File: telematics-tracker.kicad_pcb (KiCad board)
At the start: 4 copper layers, 0 parts

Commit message: M4 stage 1: board foundation - outline, mounting holes, netclasses, DRC rules
tools/pcbgen.py builds telematics-tracker.kicad_pcb from a pristine template
the same way tools/sheets.py builds the sheets. Provisional 80 x 60 mm rounded
outline, 4 corner M3 holes GND-tied, HV ZONE silk boundary at x = 20 mm.

Fifth M3 hole added at (27, 52) for F-18 - see design-log. None of the four
corner holes is usable as the IMU anchor: two sit inside the HV strip and two
in the RF corners beside the U.FL connectors. A digital-zone standoff also
stiffens the panel under the 31 x 28 mm LCC module, which matters for solder
joint life under MEWP vibration. Provisional like the outline: needs a matching
boss in the purchased housing.

Netclasses added to the project with pattern assignment (32 patterns):
  RF          track 0.40, clearance 0.30  - the computed 50 ohm CPWG geometry
  HV          track 0.50, clearance 0.60  - IPC-2221 external uncoated at 100 V
  MODEM_BULK  track 2.00                  - handoff section 4 minimum
  PWR         track 0.50
  GND         own class so the HV-to-LV rule can except it
telematics-tracker.kicad_dru adds the rules a netclass cannot express, chiefly
the directional HV-to-signal 1.5 mm separation (handoff section 7) which must
except GND, since D2/C70-C74/R80 all return to GND right beside their HV pads.

Two pcbnew traps hit and worked around, both documented in the code:
  - board.Remove() hands ownership back to Python and double-frees, segfaulting
    the interpreter on the next GC. The generator never deletes; it rebuilds
    from tools/pcb-template.kicad_pcb.
  - KIIDs are random with no Python setter, and footprints are written from an
    unordered container, so plain regeneration produced reordered blocks and
    fresh uuids every run. canonicalise() sorts top-level forms by a stable key
    and restamps uuids by position, keeping the board byte-stable so
    MIGRATION.md's "regenerate then git diff must be empty" check still works.

Veri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
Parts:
- added H1: MountingHole_3.2mm_M3_ISO7380_Pad, MountingHole_3.2mm_M3_ISO7380_Pad, F.Cu at (3.50, 3.50)
- added H2: MountingHole_3.2mm_M3_ISO7380_Pad, MountingHole_3.2mm_M3_ISO7380_Pad, F.Cu at (76.5, 3.50)
- added H3: MountingHole_3.2mm_M3_ISO7380_Pad, MountingHole_3.2mm_M3_ISO7380_Pad, F.Cu at (3.50, 56.5)
- added H4: MountingHole_3.2mm_M3_ISO7380_Pad, MountingHole_3.2mm_M3_ISO7380_Pad, F.Cu at (76.5, 56.5)
- added H5: MountingHole_3.2mm_M3_ISO7380_Pad, MountingHole_3.2mm_M3_ISO7380_Pad, F.Cu at (27.0, 52.0)
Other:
- board outline added: 80 x 60 mm
- board text added: "HV ZONE <= 100 V"

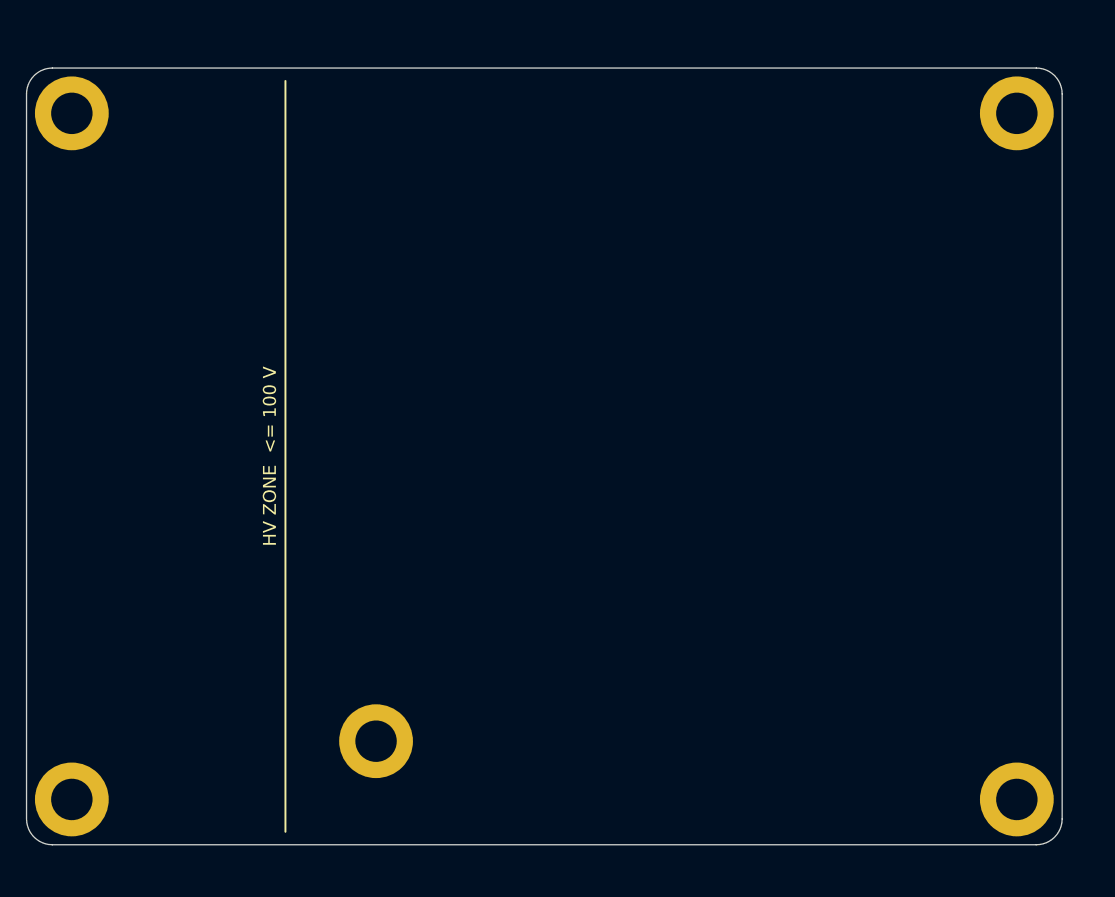
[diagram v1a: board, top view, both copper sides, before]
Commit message: M4 stage 2: F-13, F-16, F-17 closed; full placement + planes (NOT routed)
F-13 APPLIED (no waiver): VBAT_MODEM bulk 2x 100uF 6.3V X5R (C49066, which
broke rule 1 twice - X5R, and 6.3/4.35 = 1.45:1 not >=2:1) -> 4x 47uF 10V X7R
Murata GRM32ER71A476KE15L (C84494), refs C40/C41/C81/C82. 27.97uF per part read
at exact 4.35V/85.0C grid points from Murata's simulation backend = 111.9uF
effective, 2.30:1 derating. Cross-validated within ~7% by Taiyo Yuden C20486249
(second source). 10uF X5R 0805 -> C109040 X7S, +125C rated. Rule 1 now MET.
Also logged: all three previously-recorded F-13 options actually deliver only
63/76/92uF; no 100uF X7R/X7S >=10V exists in 1210/1812 from anyone; and
multiplying a 25C bias curve by a 0V temperature curve over-predicts by 9-12%.

F-17 CLOSED: derived lib/jlc.pretty/eSIM_MFF2_VFDFPN8.kicad_mod from four
independent vendor documents that publish an identical land, plus normative
ETSI TS 102 671 V12.0.0. ETSI table 6.1 confirms the schematic pinout is
correct (pins 1-8 = C5,C6,C7,C8,C4,C3,C2,C1). EP tied to GND per Infineon p.24
and numbered "1" so it merges with the GND pin. Logged as a deliberate
golden-rule-1 deviation: MFF2 is a package site, not an LCSC part, so there is
no C-number to import. This was the last unresolved footprint and the only
footprint_link_issues warning, so ERC is now 0 errors / 13 warnings.

F-16: X ambiguity RESOLVED - the incumbent's 8.50 is post-to-post centres, and
the earlier reading of 2.50/1.22 as post positions was wrong (they are the
bottom-pad chain). Y remains genuinely ambiguous. Three vendors (GCT, HRO,
Megastar) publish an identical scheme giving Y = +1.25; GCT's numbers were
re-extracted and verified locally. Megastar C7419882 (+13%) is fully
dimensioned BUT easyeda2kicad has no data for it, so switching means a
hand-drawn footprint - held for the user rather than trading a verified
imported footprint for a documented hand-drawn one. SIM area reserved with the
incumbent pad map and NO post holes, so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
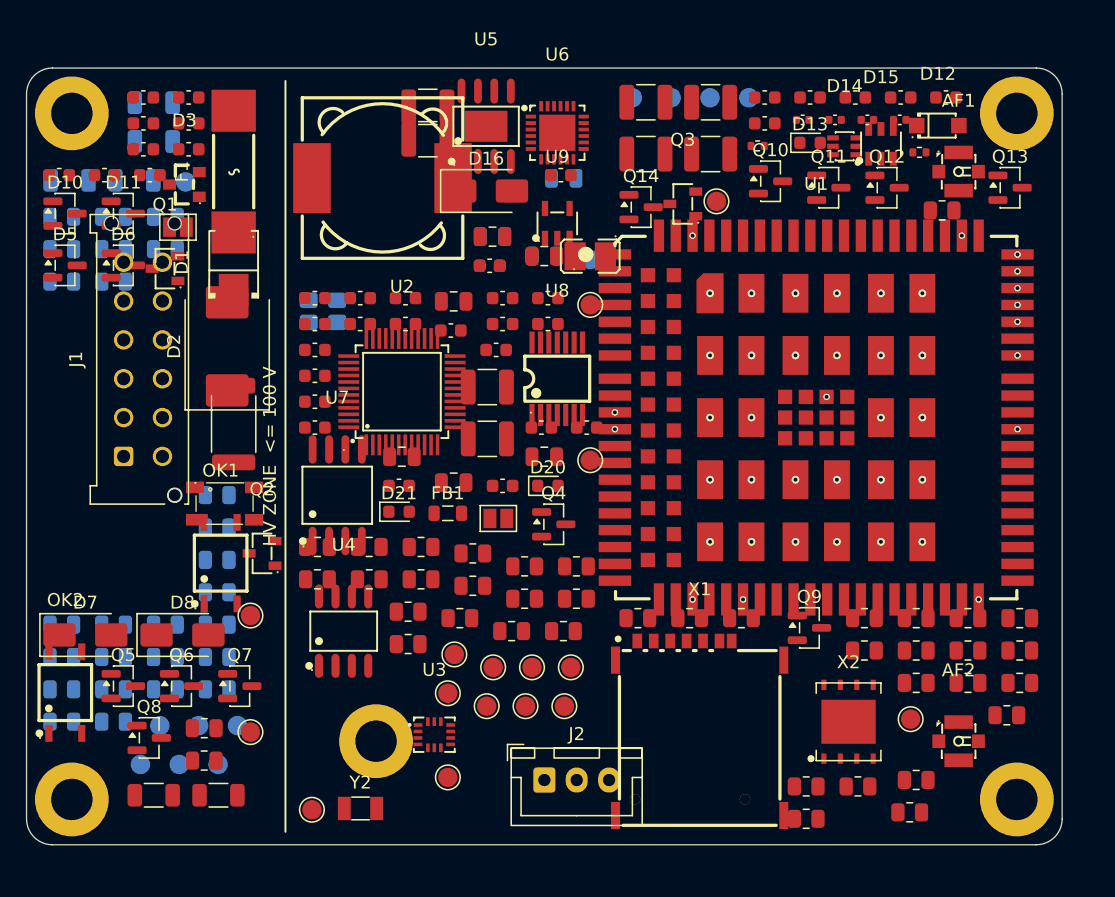
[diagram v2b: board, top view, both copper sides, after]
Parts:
- added AF2: U.FL, CONN-SMD_XY-IPEX1, F.Cu at (72.0, 52.0)
- added C1: 18pF, C_0603_1608Metric, F.Cu at (22.3, 17.8)
- added C10: 100nF, C_0603_1608Metric, F.Cu at (25.8, 17.8)
- added C11: 100nF, C_0603_1608Metric, F.Cu at (29.3, 17.8)
- added C12: 4.7uF, C_0805_2012Metric, F.Cu at (33.0, 18.0)
- added C13: 100nF, C_0603_1608Metric, F.Cu at (36.8, 17.8)
- added C14: 1uF, C_0603_1608Metric, F.Cu at (40.3, 17.8)
- added C2: 18pF, C_0603_1608Metric, F.Cu at (22.3, 19.8)
- added C20: 100nF, C_0603_1608Metric, F.Cu at (25.8, 19.8)
- added C21: 1uF, C_0603_1608Metric, F.Cu at (29.3, 19.8)
- added C22: 4.7nF, C_0603_1608Metric, F.Cu at (9.03, 2.27)
- added C23: 100nF, C_0603_1608Metric, F.Cu at (12.5, 2.27)
- added C24: 100nF, C_0603_1608Metric, F.Cu at (9.03, 4.28)
- added C25: 100nF, C_0603_1608Metric, F.Cu at (12.5, 4.28)
- added C26: 100nF, C_0603_1608Metric, F.Cu at (9.03, 6.28)
- added C27: 100nF, C_0603_1608Metric, F.Cu at (12.5, 6.28)
- added C28: 100nF, C_0603_1608Metric, F.Cu at (2.52, 8.28)
- added C29: 100nF, C_0603_1608Metric, F.Cu at (6.03, 8.28)
- added C3: 6.8pF, C_0603_1608Metric, F.Cu at (36.8, 19.8)
- added C30: 100nF, C_0603_1608Metric, F.Cu at (9.53, 8.28)
- added C4: 6.8pF, C_0603_1608Metric, F.Cu at (40.3, 19.8)
- added C40: 47uF X7R, C_1210_3225Metric, F.Cu at (47.8, 2.65)
- added C41: 47uF X7R, C_1210_3225Metric, F.Cu at (52.8, 2.65)
- added C42: 1uF, C_0603_1608Metric, F.Cu at (57.0, 2.27)
- added C43: 100nF, C_0603_1608Metric, F.Cu at (60.5, 2.27)
- added C44: 1uF, C_0603_1608Metric, F.Cu at (64.0, 2.27)
- added C45: 100nF, C_0603_1608Metric, F.Cu at (67.5, 2.27)
- added C46: 100nF, C_0603_1608Metric, F.Cu at (71.0, 2.27)
- added C47: 100nF, C_0603_1608Metric, F.Cu at (57.0, 4.28)
- added C48: DNP, C_0402_1005Metric, F.Cu at (60.0, 4.00)
- added C49: DNP, C_0402_1005Metric, F.Cu at (62.5, 4.00)
- added C5: 100nF, C_0603_1608Metric, F.Cu at (32.8, 20.3)
- added C50: DNP, C_0402_1005Metric, F.Cu at (65.0, 4.00)
- added C51: DNP, C_0402_1005Metric, F.Cu at (67.5, 4.00)
- added C6: 100nF, C_0603_1608Metric, F.Cu at (22.3, 21.8)
- added C61: 1uF, C_0603_1608Metric, F.Cu at (41.3, 8.28)
- added C62: 10uF, C_0805_2012Metric, F.Cu at (36.0, 13.0)
- added C63: 4.7uF, C_0805_2012Metric, F.Cu at (40.0, 14.5)
- added C64: 47nF, C_0603_1608Metric, F.Cu at (35.8, 15.3)
- added C65: 10uF, C_0805_2012Metric, B.Cu at (41.5, 8.53)
- added C66: 10uF, C_0805_2012Metric, B.Cu at (36.0, 13.0)
- added C67: 10uF, C_0805_2012Metric, B.Cu at (40.0, 14.5)
- added C68: 1uF, C_0603_1608Metric, B.Cu at (35.8, 15.3)
- added C69: 1uF, C_0603_1608Metric, F.Cu at (36.3, 21.8)
- added C7: 1uF, C_0603_1608Metric, F.Cu at (22.3, 23.8)
- added C70: 2.2uF 100V, C_1210_3225Metric, F.Cu at (35.6, 24.6)
- added C71: 2.2uF 100V, C_1210_3225Metric, F.Cu at (35.6, 28.6)
- added C72: 100nF, C_0603_1608Metric, F.Cu at (22.3, 25.8)
- added C73: 2.2uF 100V, C_1210_3225Metric, F.Cu at (31.0, 3.00)
- added C74: 2.2uF 100V, C_1210_3225Metric, F.Cu at (31.0, 5.50)
- added C75: 1uF 25V, C_0603_1608Metric, F.Cu at (22.3, 27.8)
- added C76: 100nF 25V, C_0603_1608Metric, F.Cu at (39.8, 27.8)
- added C77: 10uF, C_0805_2012Metric, F.Cu at (29.0, 30.0)
- added C78: 10uF, C_0805_2012Metric, F.Cu at (40.0, 30.0)
- added C79: 10uF, C_0805_2012Metric, F.Cu at (33.0, 32.0)
- added C8: 100nF, C_0603_1608Metric, F.Cu at (43.3, 27.8)
- added C80: 100nF, C_0603_1608Metric, F.Cu at (28.8, 32.3)
- added C81: 47uF X7R, C_1210_3225Metric, F.Cu at (47.8, 6.64)
- added C82: 47uF X7R, C_1210_3225Metric, F.Cu at (52.8, 6.64)
- added C9: 100nF, C_0603_1608Metric, F.Cu at (36.8, 32.3)
- added D1: S3M, SMB_L4.3-W3.6-LS5.3-RD, F.Cu at (16.0, 15.0)
- added D10: BAV99, SOT-23, F.Cu at (2.98, 11.2)
- added D11: BAV99, SOT-23, F.Cu at (7.47, 11.2)
- added D12: SMF5.0A, SOD-123FL_L2.7-W1.8-LS3.8-RD, F.Cu at (70.4, 4.45)
- added D13: NET, LED_0603_1608Metric, F.Cu at (60.5, 5.78)
- added D14: SMF05C, SOT-363_L2.0-W1.3-P0.65-LS2.1-BR, F.Cu at (63.2, 6.04)
- added D15: USBLC6-2SC6, SOT-23-6_L2.9-W1.6-P0.95-LS2.8-BL, F.Cu at (66.0, 5.86)
- added D16: SS3200, D_SMA, F.Cu at (35.5, 9.50)
- added D2: SMDJ100A, D_SMC, F.Cu at (15.5, 21.5)
- added D20: GRN, LED_0603_1608Metric, F.Cu at (40.3, 32.3)
- added D21: BLU, LED_0603_1608Metric, F.Cu at (28.8, 34.3)
- added D3: PESD1CAN, SOT-23_L2.9-W1.3-P1.90-LS2.4-BR, F.Cu at (12.2, 8.99)
- added D5: BAV99, SOT-23, F.Cu at (2.98, 15.2)
- added D6: BAV99, SOT-23, F.Cu at (7.47, 15.2)
- added D7: SS3200, D_SMA, F.Cu at (4.54, 43.8)
- added D8: SS3200, D_SMA, F.Cu at (12.0, 43.8)
- added F1: 1A 250V, FUSE-SMD_L10.1-W3.1, F.Cu at (16.0, 8.00)
- added FB1: 600R@100MHz, L_0805_2012Metric, F.Cu at (32.5, 34.4)
- added H1: MountingHole_3.2mm_M3_ISO7380_Pad, MountingHole_3.2mm_M3_ISO7380_Pad, F.Cu at (3.50, 3.50)
- added J1: WAFER-MX3.0-12PZZ, XUNPU_MX3.0-12PZZ_2x06_P3.00mm_Vertical, F.Cu at (7.50, 30.0)
- added J2: B3B-XH-A, JST_XH_B3B-XH-A_1x03_P2.50mm_Vertical, F.Cu at (40.0, 55.0)
- added JP1: BOOT0_SEL, SolderJumper-2_P1.3mm_Open_Pad1.0x1.5mm, F.Cu at (36.4, 34.8)
- added JP2: CAN_TERM, SolderJumper-2_P1.3mm_Open_Pad1.0x1.5mm, F.Cu at (11.7, 12.3)
- added L1: 150uH 2.7A, IND-SMD_L12.3-W12.3, F.Cu at (27.5, 8.50)
- added L2: ACT45B-510-2P, IND-SMD_4P-L4.5-W3.2-TL, F.Cu at (15.3, 33.6)
- added L3: 2.2uH, L1008, F.Cu at (43.5, 14.5)
- added OK1: EL357N(D), OPTO-SMD-4_L4.4-W4.1-P2.54-LS7.0-BL, F.Cu at (15.0, 38.2)
- added OK2: EL357N(D), OPTO-SMD-4_L4.4-W4.1-P2.54-LS7.0-BL, F.Cu at (3.00, 48.2)
- added Q1: AM2390N-TP, SOT-23-3_L2.9-W1.3-P1.90-LS2.4-BR, F.Cu at (10.7, 15.5)
- added Q10: MMBT3904, SOT-23, F.Cu at (57.5, 8.74)
- added Q11: MMBT3904, SOT-23, F.Cu at (62.0, 9.24)
- added Q12: MMBT3904, SOT-23, F.Cu at (66.5, 9.24)
- added Q13: MMBT3906, SOT-23, F.Cu at (76.0, 9.24)
- added Q14: MMBT3904, SOT-23, F.Cu at (47.5, 10.7)
- added Q2: AM2390N-TP, SOT-23-3_L2.9-W1.3-P1.90-LS2.4-BR, F.Cu at (18.2, 37.5)
- added Q3: AO3401A, SOT-23-3_L2.9-W1.3-P1.90-LS2.4-BR, F.Cu at (50.7, 10.5)
- added Q4: MMBT3904, SOT-23, F.Cu at (40.7, 35.2)
- added Q5: MMBT3904, SOT-23, F.Cu at (7.47, 47.7)
- added Q6: MMBT3904, SOT-23, F.Cu at (12.0, 47.7)
- added Q7: MMBT3904, SOT-23, F.Cu at (16.5, 47.7)
- added Q8: MMBT3904, SOT-23, F.Cu at (9.47, 51.7)
- added Q9: MMBT3904, SOT-23, F.Cu at (60.5, 43.2)
- added R1: 10k, R_0805_2012Metric, F.Cu at (22.5, 37.0)
- added R11: 60.4R, R_0805_2012Metric, F.Cu at (13.7, 51.0)
- added R12: 60.4R, R_0805_2012Metric, F.Cu at (13.7, 53.5)
- added R14: 12k, R_1206_3216Metric, F.Cu at (9.82, 56.2)
- added R15: 12k, R_1206_3216Metric, F.Cu at (14.8, 56.2)
- added R16: 12k, R_1206_3216Metric, B.Cu at (9.82, 2.67)
- added R17: 12k, R_1206_3216Metric, B.Cu at (9.82, 5.67)
- added R18: 12k, R_1206_3216Metric, B.Cu at (3.33, 8.68)
- added R19: 12k, R_1206_3216Metric, B.Cu at (8.32, 8.68)
- added R2: 10k, R_0805_2012Metric, F.Cu at (26.5, 37.0)
- added R21: 47k, R_0805_2012Metric, B.Cu at (2.73, 11.5)
- added R22: 47k, R_0805_2012Metric, B.Cu at (6.72, 11.5)
- added R23: 100R, R_0805_2012Metric, B.Cu at (10.7, 11.5)
- added R24: 100R, R_0805_2012Metric, B.Cu at (2.73, 14.0)
- added R25: 10k, R_0805_2012Metric, B.Cu at (6.72, 14.0)
- added R26: 10k, R_0805_2012Metric, B.Cu at (10.7, 14.0)
- added R3: 0R, R_0805_2012Metric, F.Cu at (30.5, 37.0)
- added R30: 100k, R_0805_2012Metric, B.Cu at (2.73, 16.5)
- added R31: 100k, R_0805_2012Metric, B.Cu at (6.72, 16.5)
- added R32: 100k, R_0805_2012Metric, B.Cu at (14.7, 33.0)
- added R33: 100k, R_0805_2012Metric, B.Cu at (14.7, 35.5)
- added R34: 100k, R_0805_2012Metric, B.Cu at (14.7, 38.0)
- added R35: 100k, R_0805_2012Metric, B.Cu at (14.7, 40.5)
- added R36: 9.1k, R_0805_2012Metric, B.Cu at (2.73, 43.0)
- added R37: 9.1k, R_0805_2012Metric, B.Cu at (6.72, 43.0)
- added R38: 1M, R_0805_2012Metric, B.Cu at (10.7, 43.0)
- added R39: 1M, R_0805_2012Metric, B.Cu at (14.7, 43.0)
- added R4: 1k, R_0805_2012Metric, F.Cu at (34.5, 37.5)
- added R40: 100k, R_0805_2012Metric, B.Cu at (2.73, 45.5)
- added R41: 9.1k, R_0805_2012Metric, B.Cu at (6.72, 45.5)
- added R42: 4.7k, R_0805_2012Metric, B.Cu at (10.7, 45.5)
- added R43: 10k, R_0805_2012Metric, B.Cu at (14.7, 45.5)
- added R44: 10k, R_0805_2012Metric, B.Cu at (2.73, 48.0)
- added R45: 2.2k, R_0805_2012Metric, B.Cu at (6.72, 48.0)
- added R46: 4.7k, R_0805_2012Metric, B.Cu at (10.7, 48.0)
- added R47: 10k, R_0805_2012Metric, B.Cu at (14.7, 48.0)
- added R48: 10k, R_0805_2012Metric, B.Cu at (2.73, 50.5)
- added R49: 2.2k, R_0805_2012Metric, B.Cu at (6.72, 50.5)
- added R5: 4.7k, R_0805_2012Metric, F.Cu at (38.5, 38.5)
- added R50: 100k, R_0805_2012Metric, F.Cu at (70.7, 11.0)
- added R51: 10k, R_0805_2012Metric, F.Cu at (47.2, 42.5)
- added R52: 47k, R_0805_2012Metric, F.Cu at (51.2, 42.5)
- added R53: 4.7k, R_0805_2012Metric, F.Cu at (55.2, 42.5)
- added R54: 47k, R_0805_2012Metric, F.Cu at (64.7, 42.5)
- added R55: 4.7k, R_0805_2012Metric, F.Cu at (68.7, 42.5)
- added R56: 47k, R_0805_2012Metric, F.Cu at (72.7, 42.5)
- added R57: 4.7k, R_0805_2012Metric, F.Cu at (76.7, 42.5)
- added R58: 47k, R_0805_2012Metric, F.Cu at (64.7, 45.0)
- added R59: 4.7k, R_0805_2012Metric, F.Cu at (68.7, 45.0)
- added R6: 1k, R_0805_2012Metric, F.Cu at (42.5, 38.5)
- added R60: 47k, R_0805_2012Metric, F.Cu at (72.7, 45.0)
- added R61: 47k, R_0805_2012Metric, F.Cu at (76.7, 45.0)
- added R62: 10k, R_0805_2012Metric, F.Cu at (68.7, 47.5)
- added R63: 47k, R_0805_2012Metric, F.Cu at (72.7, 47.5)
- added R64: 4.7k, R_0805_2012Metric, F.Cu at (76.7, 47.5)
- added R65: 1k, R_0805_2012Metric, F.Cu at (75.7, 50.0)
- added R66: 33R, R_0805_2012Metric, F.Cu at (68.7, 55.0)
- added R67: 33R, R_0805_2012Metric, F.Cu at (60.2, 55.5)
- added R68: 33R, R_0805_2012Metric, F.Cu at (64.2, 55.5)
- added R69: 0R, R_0805_2012Metric, F.Cu at (68.2, 57.5)
- added R7: 2.2k, R_0805_2012Metric, F.Cu at (22.5, 39.5)
- added R70: 0R, R_0805_2012Metric, F.Cu at (60.2, 58.0)
- added R71: 0R, R_0402_1005Metric, F.Cu at (56.5, 6.01)
- added R72: 0R, R_0402_1005Metric, F.Cu at (69.0, 6.51)
- added R8: 2.2k, R_0805_2012Metric, F.Cu at (26.5, 39.5)
- added R80: 1R 2512 anti-surge, R_2512_6332Metric, F.Cu at (16.0, 27.5)
- added R81: 100k, R_0805_2012Metric, F.Cu at (30.5, 39.5)
- added R82: 0R (F-12), R_0805_2012Metric, F.Cu at (34.5, 40.0)
- added R83: 4.3k, R_0805_2012Metric, F.Cu at (38.5, 41.0)
- added R84: 1.5k, R_0805_2012Metric, F.Cu at (42.5, 41.0)
- added R85: 976R, R_0805_2012Metric, F.Cu at (29.5, 42.0)
- added R86: 536R, R_0805_2012Metric, F.Cu at (33.5, 42.5)
- added R87: 10k, R_0805_2012Metric, F.Cu at (37.5, 43.5)
- added R88: 5.23k, R_0805_2012Metric, F.Cu at (41.5, 43.5)
- added R89: 30.1k, R_0805_2012Metric, F.Cu at (29.5, 44.5)
- added TP1: SWDIO, TestPoint_Pad_D1.5mm, F.Cu at (43.5, 18.3)
- added TP10: VIN_SENSE, TestPoint_Pad_D1.5mm, F.Cu at (17.3, 42.3)
- added TP11: IGN_SENSE, TestPoint_Pad_D1.5mm, F.Cu at (17.3, 51.3)
- added TP12: VBAT_SENSE, TestPoint_Pad_D1.5mm, B.Cu at (12.3, 8.80)
- added TP13: SYS, TestPoint_Pad_D1.5mm, B.Cu at (10.3, 50.8)
- added TP14: MODEM_STATUS, TestPoint_Pad_D1.5mm, F.Cu at (53.3, 10.3)
- added TP15: USB_DP_TP, TestPoint_Pad_D1.5mm, F.Cu at (68.3, 50.3)
- added TP16: USB_DM_TP, TestPoint_Pad_D1.5mm, B.Cu at (46.8, 2.30)
- added TP17: USB_VBUS, TestPoint_Pad_D1.5mm, B.Cu at (49.8, 2.30)
- added TP18: GND, TestPoint_Pad_D1.5mm, B.Cu at (52.8, 2.30)
- added TP19: 5V0, TestPoint_Pad_D1.5mm, B.Cu at (43.5, 14.8)
- added TP2: SWCLK, TestPoint_Pad_D1.5mm, F.Cu at (43.5, 30.3)
- added TP20: SYS, TestPoint_Pad_D1.5mm, F.Cu at (33.0, 45.3)
- added TP21: U6_STAT, TestPoint_Pad_D1.5mm, F.Cu at (36.0, 46.3)
- added TP22: U6_PG, TestPoint_Pad_D1.5mm, F.Cu at (39.0, 46.3)
- added TP23: VIN, TestPoint_Pad_D1.5mm, B.Cu at (13.3, 50.8)
- added TP24: VBAT_MODEM, TestPoint_Pad_D1.5mm, B.Cu at (55.8, 2.30)
- added TP25: CANH, TestPoint_Pad_D1.5mm, B.Cu at (16.3, 50.8)
- added TP26: CANL, TestPoint_Pad_D1.5mm, B.Cu at (8.80, 53.8)
- added TP27: MODEM_TX, TestPoint_Pad_D1.5mm, F.Cu at (42.0, 46.3)
- added TP28: MODEM_RX, TestPoint_Pad_D1.5mm, F.Cu at (32.5, 48.3)
- added TP3: NRST, TestPoint_Pad_D1.5mm, F.Cu at (35.5, 49.3)
- added TP4: DBG_TX, TestPoint_Pad_D1.5mm, F.Cu at (38.5, 49.3)
- added TP5: DBG_RX, TestPoint_Pad_D1.5mm, F.Cu at (41.5, 49.3)
- added TP6: 3V3, TestPoint_Pad_D1.5mm, F.Cu at (32.5, 54.8)
- added TP7: GND, TestPoint_Pad_D1.5mm, F.Cu at (22.0, 57.3)
- added TP8: J1_SPARE1, TestPoint_Pad_D1.5mm, B.Cu at (11.8, 53.8)
- added TP9: J1_SPARE2, TestPoint_Pad_D1.5mm, B.Cu at (14.8, 53.8)
- added U1: EC200UCNAA-N05-SGNSA, LCC-LGA-144_L31.0-W28.0-P1.30_L610-CN-02, F.Cu at (61.0, 27.0)
- added U2: AT32F403ACGT7, LQFP-48_L7.0-W7.0-P0.50-LS9.0-BL_1, F.Cu at (29.0, 25.0)
- added U3: QMI8658B, LGA-14_L3.0-W2.5-P0.50-TL, F.Cu at (31.5, 51.5)
- added U4: SIT1051AT/3, SOP-8_L4.9-W3.9-P1.27-LS6.0-BL, F.Cu at (24.5, 43.5)
- added U5: EG11752, SOIC-8_L4.9-W3.9-P1.27-LS6.0-BL-EP3.3-1, F.Cu at (35.5, 4.50)
- added U6: BQ25606RGER, VQFN-24_L4.0-W4.0-P0.50-TL-EP2.8, F.Cu at (41.0, 5.00)
- added U7: GD25Q64ESIGR, SOP-8_L5.3-W5.3-P1.27-LS8.0-BL, F.Cu at (24.0, 33.0)
- added U8: TXB0104PWR, TSSOP-14_L5.0-W4.4-P0.65-LS6.4-BL, F.Cu at (41.0, 24.0)
- added U9: ME6211C33M5G, SOT-23-5_L3.0-W1.7-P0.95-LS2.8-BL, F.Cu at (41.0, 12.0)
- added X1: NANO-SIM, SIM-SMD_YKSIM-PUSH137-140NANO, F.Cu at (52.0, 51.0)
- added X2: MFF2-eSIM-pads, eSIM_MFF2_VFDFPN8, F.Cu at (63.5, 50.5)
- added Y1: 8MHz, Crystal_SMD_3225-4Pin_3.2x2.5mm, B.Cu at (22.9, 18.8)
- added Y2: 32.768kHz, Crystal_SMD_3215-2Pin_3.2x1.5mm, F.Cu at (25.8, 57.2)
- AF1: renamed from H1; value MountingHole_3.2mm_M3_ISO7380_Pad -> U.FL; footprint MountingHole_3.2mm_M3_ISO7380_Pad -> CONN-SMD_XY-IPEX1
- moved AF1 68.6 mm to (72.0, 8.00)
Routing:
- net GND: vias 0 -> 43
- added copper zone on In2.Cu, net 3V3
- added copper zone on In2.Cu, net 5V0
- added copper zone on In1.Cu, net GND
- added copper zone on In2.Cu, net SYS

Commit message: M4 Option 4: floorplan complete for review - 896 -> 518 DRC, all 218 placed
Placement, L2 GND, L3 pours, HV keepout and thermal vias done. NOT ROUTED -
that is Option 1, gated on floorplan approval. tools/build.py runs the whole
build in the one order that works; byte-identical across consecutive builds.

Shorting items 51->0, solder mask bridges 71->0, courtyard overlaps 22->3,
annular/padstack 17/2->0/0, hole-to-hole and dangling vias 7/9->0/0, silk
398->38, components placed 214->218 of 218. Of 24 remaining clearance items,
23 are justified waivers, classified in docs/drc-exceptions.md.

Six real bugs found and fixed:
- GetCourtyard() can be smaller than the pad extent: U2's LQFP-48 courtyard
  reads 7.1x7.1 (body) while its pads reach 9.0mm, so 0603s were packed onto
  its leads. Keepout is now max(courtyard, pads).
- The keepout box was centred on the footprint ORIGIN, not the box. J1's
  derived Molex courtyard is centred 7.50/1.92mm off its origin (origin is on
  pin 1), so a correct-sized box was blocked in the wrong place.
- FindPadByNumber() returns only the first pad with that number, so the MFF2
  exposed pad (deliberately numbered "1") never got a net and DRC read it as a
  short against its twin.
- Zones were filled before net classes existed, so the fill used Default
  0.2mm where HV needs 0.6mm and flagged the GND plane against every J1 pad.
- pcbnew.SaveBoard() WIPES net_settings from the project, so the generators
  were destroying the net classes every run - RF/HV/MODEM_BULK silently
  stopped applying while DRC still looked like it passed them.
- Hand-written netclass dicts are silently discarded by KiCad unless they
  carry bus_width/priority/tuning_profile with meta.version 5. All five
  classes had already reverted to just "Default" in a previous commit.
  tools/netclasses.py now verifies they survive a KiCad round trip.

F-16 CLOSED: the imported SIM footprint already contained the locating-post
holes, and they match the GCT/HRO/Megastar cons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
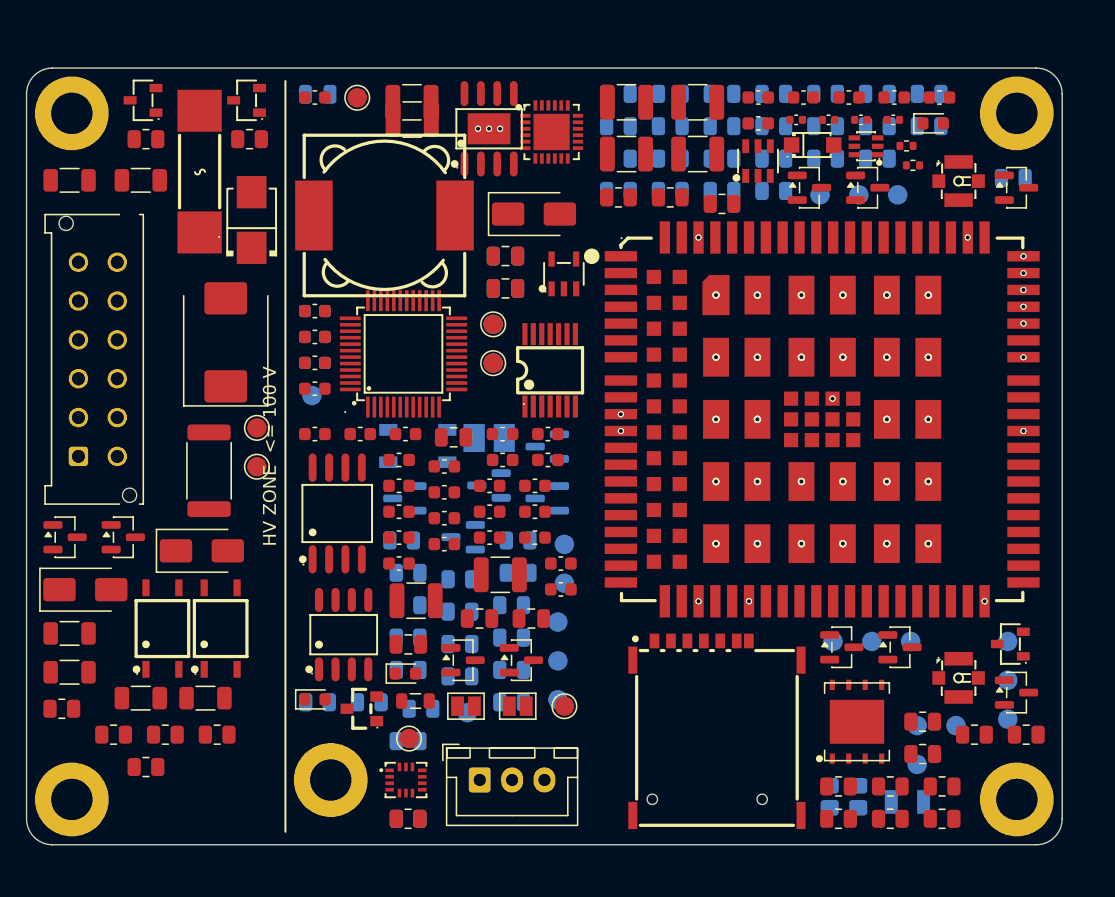
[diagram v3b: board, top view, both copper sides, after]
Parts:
- C68, R16, R17, R18, R19, R30, R31, R32, R33, R34, R35, R40, R46, R47, R48, R49, TP19, TP8, TP9: moved to F.Cu
- C75, C76, C80, L2, L3, Q4, Q5, Q6, Q7, Q8, R11, R12, R2, R3, R4, R58, R59, R6, R60, R61, R62, R63, R64, R65, R66, R67, R68, R69, R7, R70, R8, R81, R82, R83, R84, R85, R86, R87, R88, R89, TP11, TP14, TP15, TP2, TP22, TP27, TP28, TP3, TP4, TP5, TP6, TP7, Y2: moved to B.Cu
- moved R48 64.8 mm to (53.7, 10.5), turned to 0 degrees
- moved R49 62.5 mm to (69.2, 50.5), turned to 0 degrees
- moved R7 58.8 mm to (69.7, 4.50), turned to 180 degrees
- moved R85 57.5 mm to (76.2, 8.49), turned to 180 degrees
- moved Y1 55.0 mm to (63.1, 56.3)
- moved R69 53.1 mm to (65.7, 4.50), turned to 180 degrees
- moved R70 53.0 mm to (45.7, 7.00), turned to 180 degrees
- moved R64 53.0 mm to (45.7, 4.50), turned to 180 degrees
- moved R66 52.7 mm to (53.7, 4.50), turned to 180 degrees
- moved R65 52.4 mm to (49.7, 4.50), turned to 180 degrees
- moved R46 51.7 mm to (45.7, 9.99), turned to 0 degrees
- moved R47 51.7 mm to (49.7, 9.99), turned to 0 degrees
- moved R67 51.1 mm to (57.7, 4.50), turned to 180 degrees
- moved R68 51.1 mm to (61.7, 4.50), turned to 180 degrees
- moved R14 47.9 mm to (3.33, 8.68)
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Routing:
- net /power/VIN_B: vias 0 -> 3
- added copper zone on In2.Cu, net /power/VIN_B
